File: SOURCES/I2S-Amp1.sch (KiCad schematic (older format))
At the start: 48 parts, among them P2 CONN_01X02, P3 CONN_01X02, P4 CONN_01X02, U1 SN74LVC14ADG4, U2 LM317_SOT223, U3 TAS5760MDCAR

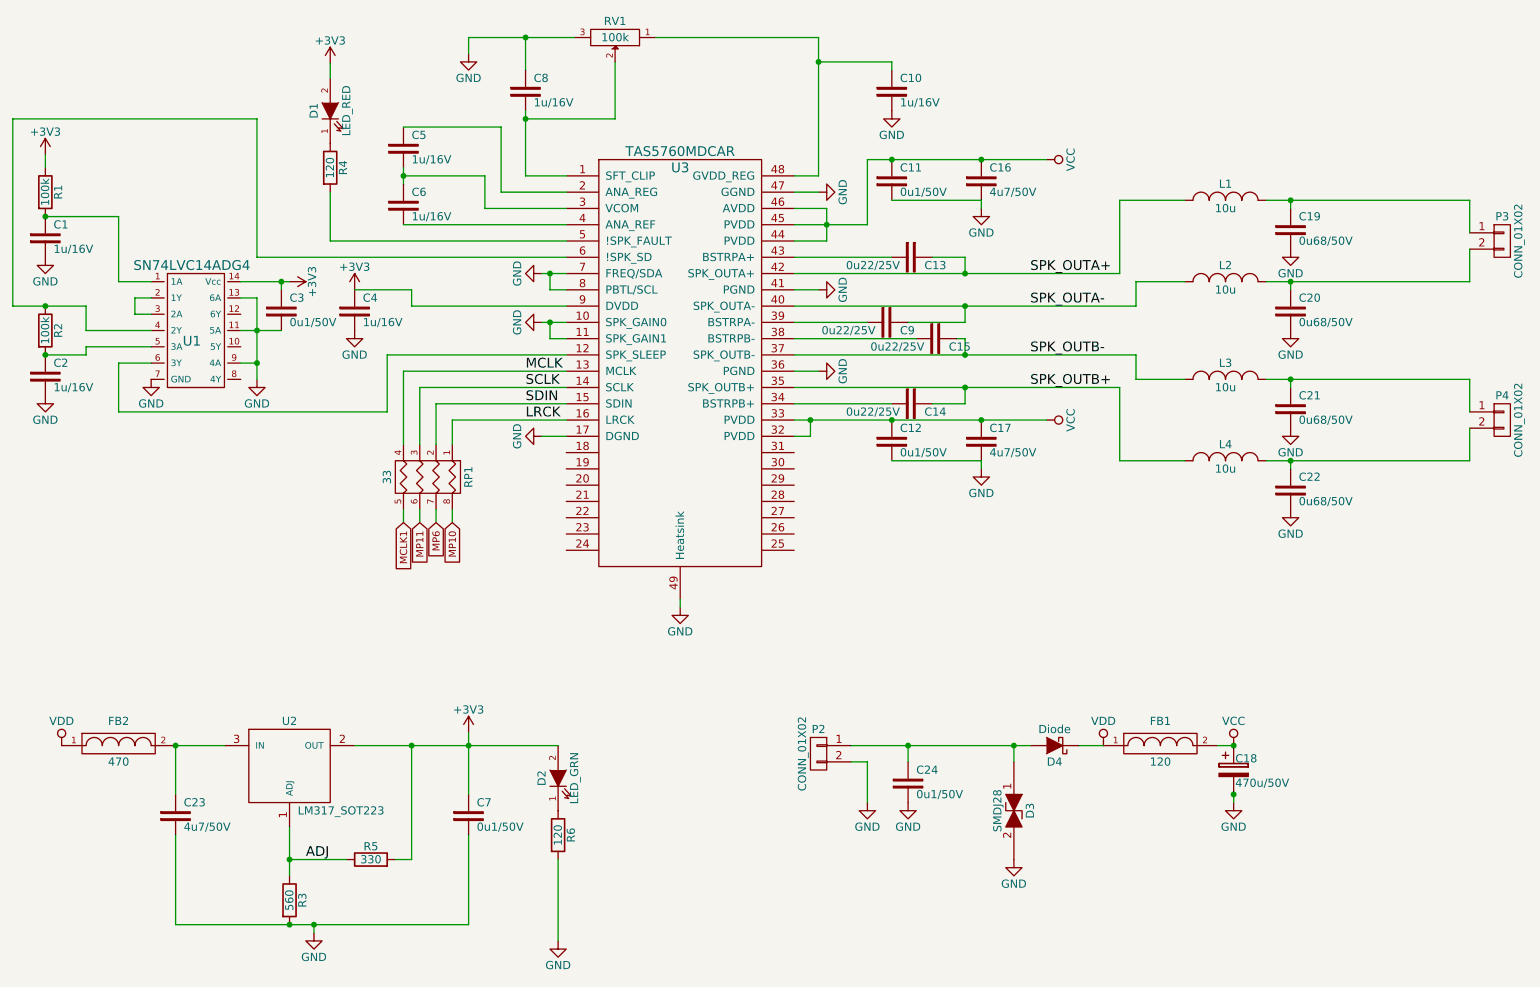
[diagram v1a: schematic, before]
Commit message: added analog input
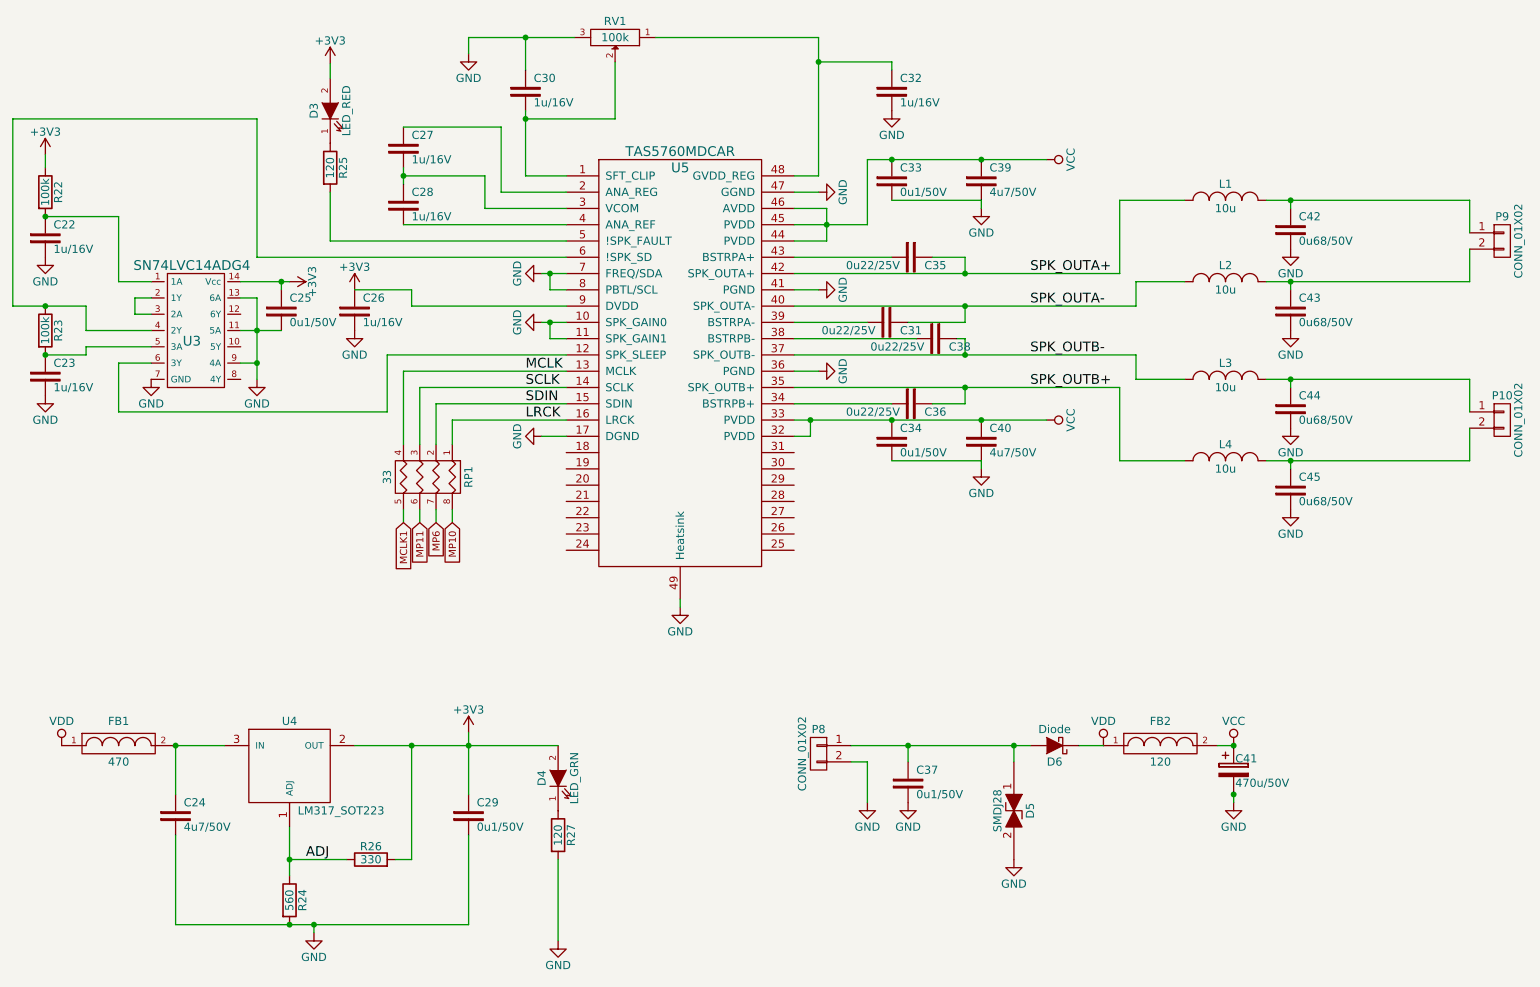
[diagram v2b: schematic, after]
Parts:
- removed C13, C14, C15, C9: 0u22/25V, Capacitors_SMD:C_0603, symbol Capacitor
- removed C16: 4u7/50V, Capacitors_SMD:C_1206, symbol Capacitor
- removed C18: 470u/50V, Capacitors_ThroughHole:C_Radial_D10_L16_P5, symbol CP
- removed C2, C4, C5, C6: 1u/16V, Capacitors_SMD:C_0603, symbol Capacitor
- removed C20, C22: 0u68/50V, Capacitors_SMD:C_1206, symbol Capacitor
- removed D1: LED_RED, LEDs:LED_0603, symbol LED
- removed D2: LED_GRN, LEDs:LED_0603, symbol LED
- removed D3: SMDJ28, Diodes_SMD:DO-214AB, symbol TVS
- removed D4: Diode, MyFootprints:PowerDI5, symbol D_Schottky
- removed P2, P3: CONN_01X02, MyFootprints:Connector0.5, symbol CONN_01X02
- removed R1, R2: 100k, Resistors_SMD:R_0603, symbol R
- removed U1: SN74LVC14ADG4, Housings_SOIC:SOIC-14_3.9x8.7mm_Pitch1.27mm, symbol SN74LVC14ADG4
- added C26, C27, C28: 1u/16V, Capacitors_SMD:C_0603, symbol Capacitor
- added C31, C35, C36, C38: 0u22/25V, Capacitors_SMD:C_0603, symbol Capacitor
- added C37: 0u1/50V, Capacitors_SMD:C_0603, symbol Capacitor
- added C39: 4u7/50V, Capacitors_SMD:C_1206, symbol Capacitor
- added C41: 470u/50V, Capacitors_ThroughHole:C_Radial_D10_L16_P5, symbol CP
- added C43, C45: 0u68/50V, Capacitors_SMD:C_1206, symbol Capacitor
- added D3: LED_RED, LEDs:LED_0603, symbol LED
- added D4: LED_GRN, LEDs:LED_0603, symbol LED
- added D5: SMDJ28, Diodes_SMD:DO-214AB, symbol TVS
- added D6: Diode, MyFootprints:PowerDI5, symbol D_Schottky
- added P8, P9: CONN_01X02, MyFootprints:Connector0.5, symbol CONN_01X02
- added R22, R23: 100k, Resistors_SMD:R_0603, symbol R
- added U3: SN74LVC14ADG4, Housings_SOIC:SOIC-14_3.9x8.7mm_Pitch1.27mm, symbol SN74LVC14ADG4
- C23: value 4u7/50V -> 1u/16V; footprint Capacitors_SMD:C_1206 -> Capacitors_SMD:C_0603; Mfr.Nr. GRM31CR71H475KA12L -> GRM188R71C105KE15D
- C24: value 0u1/50V -> 4u7/50V; footprint Capacitors_SMD:C_0603 -> Capacitors_SMD:C_1206; Mfr.Nr. GRM188R71H104KA93D -> GRM31CR71H475KA12L
- FB1: value 120 -> 470; footprint Capacitors_SMD:C_1206 -> Capacitors_SMD:C_0603; Mfr.Nr. BLM31PG121SN1L -> BLM18PG471SN1D
- FB2: value 470 -> 120; footprint Capacitors_SMD:C_0603 -> Capacitors_SMD:C_1206; Mfr.Nr. BLM18PG471SN1D -> BLM31PG121SN1L
- renumbered C1 to C22, C3 to C25, C7 to C29, C8 to C30, C10 to C32, C11 to C33, C12 to C34, C17 to C40, C19 to C42, C21 to C44, P4 to P10, R3 to R24, R4 to R25, R5 to R26, R6 to R27, U2 to U4, U3 to U5
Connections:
- net +3V3: now also C26.1, D3.2 (A), D4.2 (A), R22.1, U3.14 (Vcc)
- net GND: now also C26.2, C37.2, C39.2, C41.2, C43.2, C45.2, D5.2, P8.2 (P2), U3.11 (5A), U3.13 (6A), U3.7 (GND), U3.9 (4A)
- net SPK_OUTA+: now also C35.1
- net SPK_OUTA-: now also C31.1
- net SPK_OUTB+: now also C36.1
- net SPK_OUTB-: now also C38.1
- net VCC: now also FB2.2, C39.1, C41.1; no longer FB1.2
- net VDD: now also D6.1 (K)
- net at U5.12 (SPK_SLEEP): now also U3.6 (3Y)
- net at U5.2 (ANA_REG): now also C27.1
- net at U5.3 (VCOM): now also C27.2, C28.1
- net at U5.34 (BSTRPB+): now also C36.2
- net at U5.38 (BSTRPB-): now also C38.2
- net at U5.39 (BSTRPA-): now also C31.2
- net at U5.4 (ANA_REF): now also C28.2
- net at U5.43 (BSTRPA+): now also C35.2
- net at U5.6 (!SPK_SD): now also R23.1, U3.4 (2Y)
- net at C42.1, L1.2: now also P9.1 (P1)
- net at L2.2: now also C43.1, P9.2 (P2)
- net at L4.2, P10.2 (P2): now also C45.1
- net at R25.1: now also D3.1 (K)
- net at C22.1: now also R22.2, U3.1 (1A)
- net at R27.1: now also D4.1 (K)
- net at C24.1: now also FB1.2, U4.3 (IN)
- new net: U3.2 (1Y), U3.3 (2A)
- new net: C23.1, R23.2, U3.5 (3A)
- new net: C37.1, D5.1, D6.2 (A), P8.1 (P1)

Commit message: added power
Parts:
- C25, C33, C34: value 0u1/50V -> 0u1/35V
- C39, C40: value 4u7/50V -> 4u7/35V
- C42, C43, C44, C45: value 0u68/50V -> 0u68/35V

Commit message: modifications amp
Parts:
- removed C24: 4u7/50V, Capacitors_SMD:C_1206, symbol Capacitor
- removed C29, C37: 0u1/50V, Capacitors_SMD:C_0603, symbol Capacitor
- removed C41: 470u/50V, Capacitors_ThroughHole:C_Radial_D10_L16_P5, symbol CP
- removed D4: LED_GRN, LEDs:LED_0603, symbol LED
- removed D5: SMDJ28, Diodes_SMD:DO-214AB, symbol TVS
- removed D6: Diode, MyFootprints:PowerDI5, symbol D_Schottky
- removed FB1: 470, Capacitors_SMD:C_0603, symbol FILTER
- removed FB2: 120, Capacitors_SMD:C_1206, symbol FILTER
- removed P8: CONN_01X02, MyFootprints:Connector0.5, symbol CONN_01X02
- removed R24: 560, Resistors_SMD:R_0603, symbol R
- removed R26: 330, Resistors_SMD:R_0603, symbol R
- removed R27: 120, Resistors_SMD:R_0603, symbol R
- removed RP1: 33, Resistors_SMD:R_Array_Concave_4x0603, symbol R_PACK4
- removed U4: LM317_SOT223, TO_SOT_Packages_SMD:SOT-223, symbol LM317_SOT223
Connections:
- net LRCK is gone; now on net MP10: U5.16 (LRCK)
- net MCLK is gone; now on net MCLK1: U5.13 (MCLK)
- net SCLK is gone; now on net MP11: U5.14 (SCLK)
- net SDIN is gone; now on net MP6: U5.15 (SDIN)

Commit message: design rule check
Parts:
- renumbered C25 to C24, C26 to C25, C27 to C26, C28 to C27, C30 to C28, C31 to C29, C32 to C30, C33 to C31, C34 to C32, C35 to C33, C36 to C34, C38 to C35, C39 to C36, C40 to C37, C42 to C38, C43 to C39, C44 to C40, C45 to C41, R25 to R24, U5 to U4

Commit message: design rule check
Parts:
- U4: footprint MyFootprints:HTSSOP-48 -> (none); Mfr.Nr. TAS5760MDCA -> (none)
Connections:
- no-connect marks 0 -> 17
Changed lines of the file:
@@
 LIBS:fdsp_transistor_new
 LIBS:LM2738XMY&slash_NOPB-symbols
+LIBS:smd_aio-cache
 EELAYER 25 0
 EELAYER END
@@
 $EndDescr
 $Comp
-L TAS5760MDCAR U4
-U 1 1 574C04F8
-P 5750 3050
-F 0 "U4" H 5750 4250 60  0000 C CNN
-F 1 "TAS5760MDCAR" H 5750 4350 60  0000 C CNN
-F 2 "MyFootprints:HTSSOP-48" H 5650 2950 60  0001 C CNN
-F 3 "http://www.mouser.com/ds/2/405/tas5760m-480127.pdf" H 5750 3050 60  0001 C CNN
-F 4 "TAS5760MDCA" H 5750 3050 60  0001 C CNN "Mfr.Nr."
-	1    5750 3050
-	1    0    0    -1
-$EndComp
-$Comp
 L POT RV1
 U 1 1 574C1518
@@
 Text GLabel 4050 3630 3    44   Input ~ 0
 MCLK1
+NoConn ~ 5050 3600
+NoConn ~ 5050 3700
+NoConn ~ 5050 3800
+NoConn ~ 5050 3900
+NoConn ~ 5050 4000
+NoConn ~ 5050 4100
+NoConn ~ 5050 4200
+NoConn ~ 6450 3700
+NoConn ~ 6450 3800
+NoConn ~ 6450 3900
+NoConn ~ 6450 4000
+NoConn ~ 6450 4100
+NoConn ~ 6450 4200
+NoConn ~ 3050 2750
+NoConn ~ 3050 2950
+NoConn ~ 3050 3150
+$Comp
+L TAS5760MDCAR U4
+U 1 1 5B18AD92
+P 5750 3050
+F 0 "U4" H 5950 1750 60  0000 C TNN
+F 1 "TAS5760MDCAR" H 5750 4350 60  0000 C CNN
+F 2 "" H 5850 2950 60  0000 C CNN
+F 3 "" H 5750 3050 60  0000 C CNN
+	1    5750 3050
+	1    0    0    -1
+$EndComp
+NoConn ~ 6450 3600
 $EndSCHEMATC
